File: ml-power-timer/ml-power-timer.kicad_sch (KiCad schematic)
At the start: 16 parts, among them U1 TLC555 (TURN ON), U2 TLC555 (TURN OFF; DELAY)

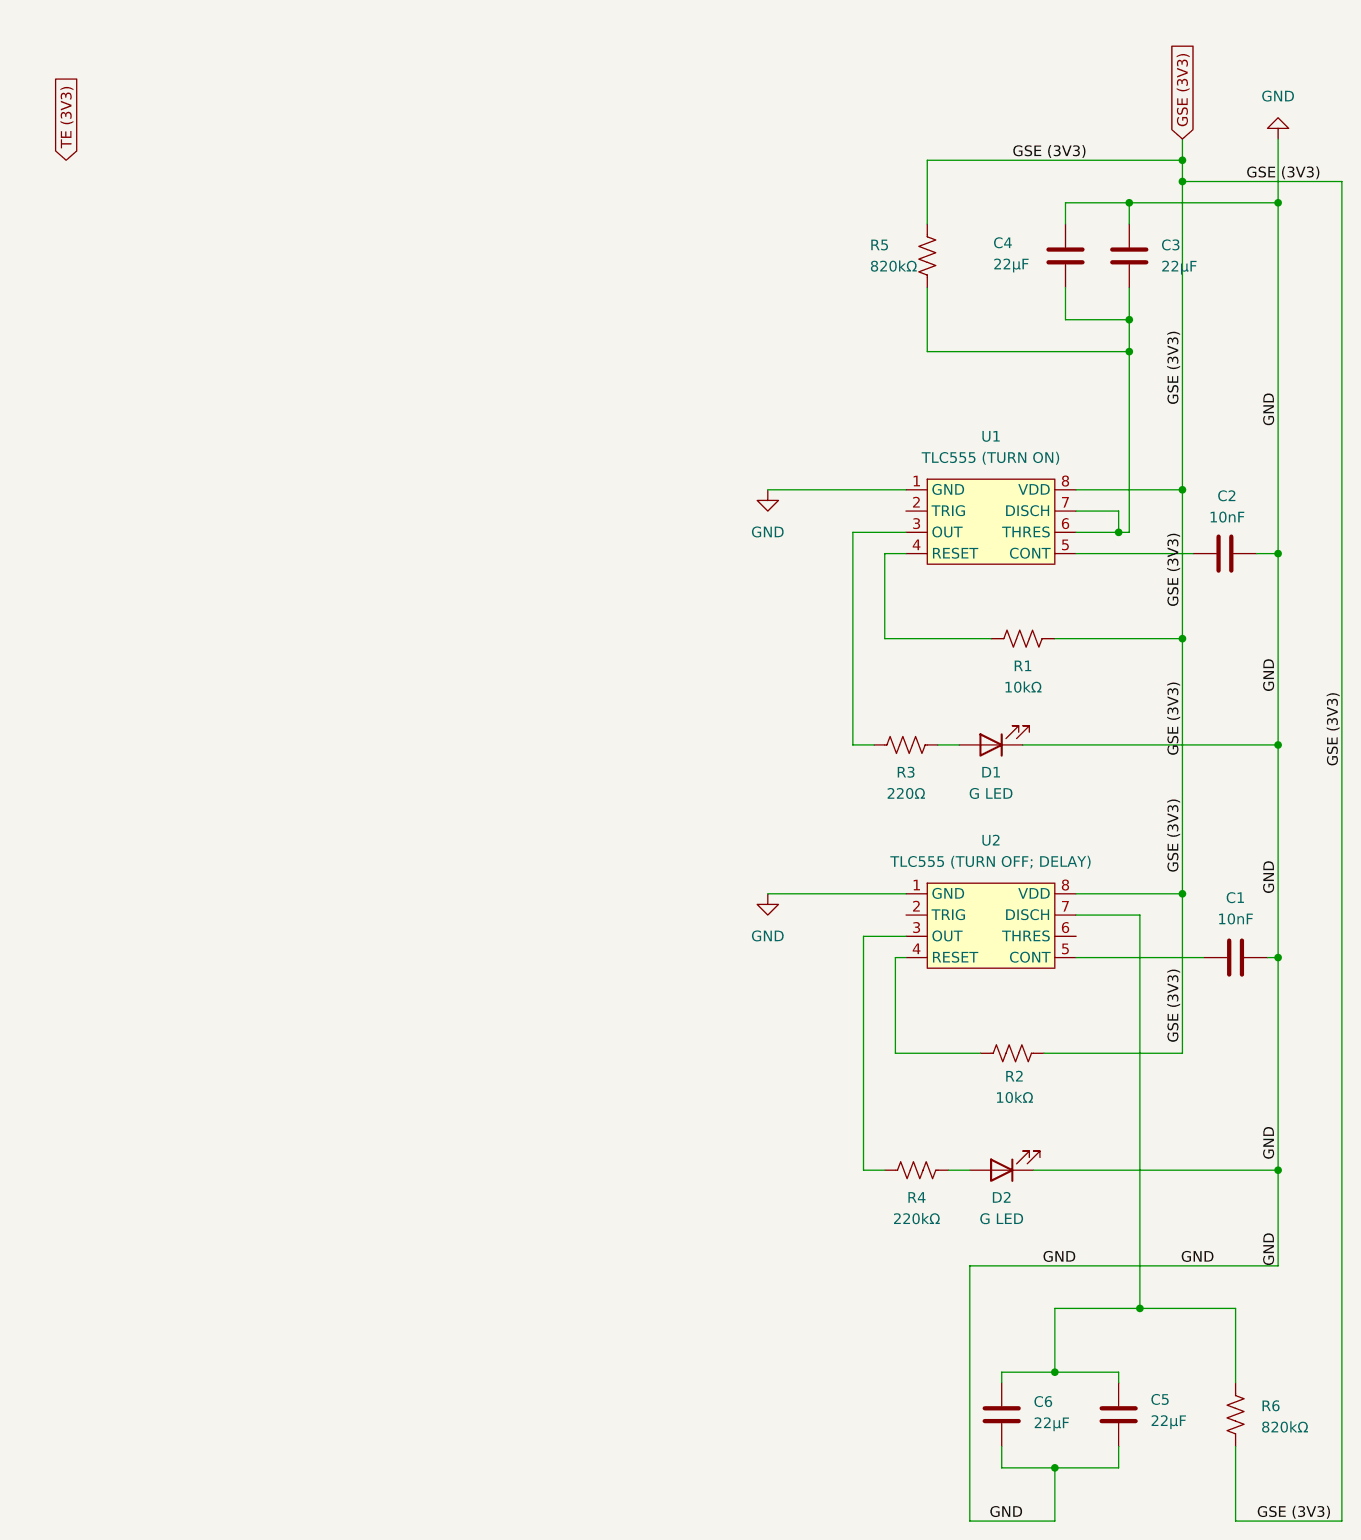
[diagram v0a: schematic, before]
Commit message: Updated schematic for breadboard
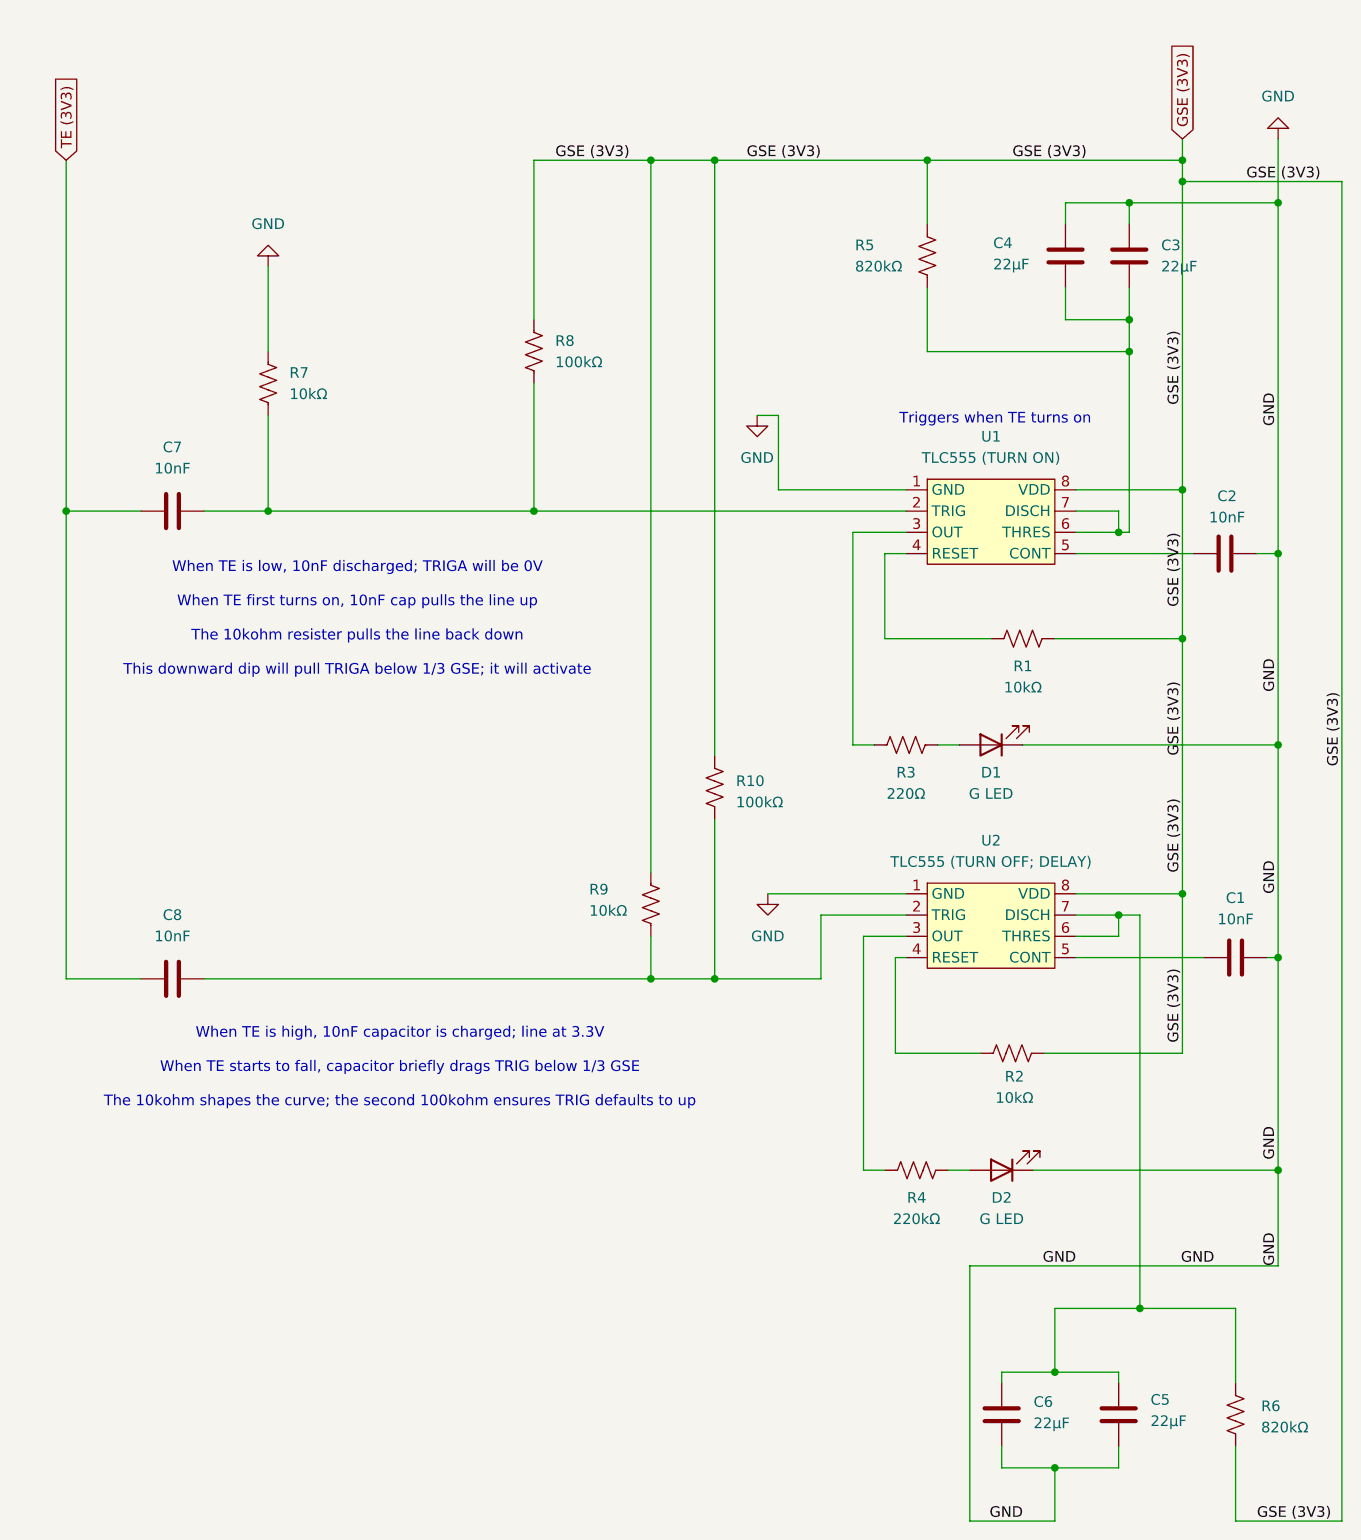
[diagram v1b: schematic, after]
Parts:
- added C7, C8: 10nF, symbol Device:C
- added R10, R8: 100kΩ, symbol Device:R_US
- added R7, R9: 10kΩ, symbol Device:R_US
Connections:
- net GND: now also R7.1
- net GSE (3V3): now also R10.1, R8.1, R9.1
- net TE (3V3): now also C7.1, C8.1
- net at U1.2 (TRIG): now also C7.2, R7.2, R8.2
- net at C5.1, C6.1, R6.1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: now also U2.6 (THRES)
- net at U2.2 (TRIG): now also C8.2, R10.2, R9.2
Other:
- note added: "Triggers when TE turns on"
- note added: "When TE is high, 10nF capacitor is charged; line at 3.3V When TE starts to fall, capacitor briefly drags TRIG below 1/3 GSE The 10kohm shapes the curve; the second 100kohm ensures TRIG defaults to up"
- note added: "When TE is low, 10nF discharged; TRIGA will be 0V When TE first turns on, 10nF cap pulls the line up The 10kohm resister pulls the line back down This downward dip will pull TRIGA below 1/3 GSE; it will activate"

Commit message: Added Red Generation PCB
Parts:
- D2: value G LED -> R LED
- R4: value 220kΩ -> 220Ω
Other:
- note added: "Triggers when TE turns off"
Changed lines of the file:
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@@
+		)
+	)
+	(text "Triggers when TE turns off"
+		(exclude_from_sim no)
+		(at 104.14 161.798 0)
+		(effects
+			(font
+				(size 1.27 1.27)
+			)
 		)
 	)
@@
 			)
 		)
-		(property "Value" "G LED"
+		(property "Value" "R LED"
 			(at 129.54 156.972 0)
 			(effects
@@
 			)
 		)
-		(property "Value" "220kΩ"
+		(property "Value" "220Ω"
 			(at 119.38 156.972 90)
 			(effects
